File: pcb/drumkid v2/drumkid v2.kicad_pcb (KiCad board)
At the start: 2 copper layers, 0 parts

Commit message: more pcb changes, about to do a big-ish change so doing a commit now
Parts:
- added BT1: Battery, Connector_PinHeader_2.54mm:PinHeader_1x02_P2.54mm_Vertical, F.Cu at (162.0, 128.0)
- added C1: 150uF, Capacitor_THT:CP_Radial_D6.3mm_P2.50mm, F.Cu at (137.0, 64.0)
- added C10: 220uF, Capacitor_THT:CP_Radial_D6.3mm_P2.50mm, F.Cu at (102.0, 71.0)
- added C2: 0.1uF, Capacitor_THT:C_Disc_D3.4mm_W2.1mm_P2.50mm, F.Cu at (150.0, 55.0)
- added C3: 100uF, Capacitor_THT:CP_Radial_D6.3mm_P2.50mm, F.Cu at (137.0, 56.0)
- added C4: 0.1uF, Capacitor_THT:C_Disc_D3.4mm_W2.1mm_P2.50mm, F.Cu at (113.0, 53.0)
- added C5: 10uF, Capacitor_THT:C_Disc_D3.4mm_W2.1mm_P2.50mm, F.Cu at (142.0, 84.0)
- added C6: 10uF, Capacitor_THT:C_Disc_D3.4mm_W2.1mm_P2.50mm, F.Cu at (147.0, 84.0)
- added C7: 10uF, Capacitor_THT:CP_Radial_D6.3mm_P2.50mm, F.Cu at (114.0, 60.0)
- added C8: 100uF, Capacitor_THT:CP_Radial_D6.3mm_P2.50mm, F.Cu at (94.0, 71.0)
- added C9: 0.1uF, Capacitor_THT:C_Disc_D3.4mm_W2.1mm_P2.50mm, F.Cu at (92.0, 79.0)
- added D1: 1N5817, Diode_THT:D_DO-41_SOD81_P10.16mm_Horizontal, F.Cu at (144.0, 65.0)
- added D2: LED, LED_THT:LED_D5.0mm, F.Cu at (151.0, 72.0)
- added D3: LED, LED_THT:LED_D5.0mm, F.Cu at (111.0, 72.0)
- added D4: LED, LED_THT:LED_D5.0mm, F.Cu at (121.0, 72.0)
- added D5: LED, LED_THT:LED_D5.0mm, F.Cu at (131.0, 72.0)
- added D6: LED, LED_THT:LED_D5.0mm, F.Cu at (141.0, 72.0)
- added J1: Conn_01x03_Female, Connector_PinHeader_2.54mm:PinHeader_1x03_P2.54mm_Vertical, F.Cu at (169.0, 67.7)
- added J2: Conn_01x03_Female, Connector_PinHeader_2.54mm:PinHeader_1x03_P2.54mm_Vertical, F.Cu at (154.0, 63.0)
- added J3: Conn_01x03_Female, Connector_PinHeader_2.54mm:PinHeader_1x03_P2.54mm_Vertical, F.Cu at (169.0, 64.0)
- added J4: Conn_01x03_Female, Connector_PinHeader_2.54mm:PinHeader_1x03_P2.54mm_Vertical, F.Cu at (154.1, 66.0)
- added J5: Conn_01x05_Female, Connector_PinHeader_2.54mm:PinHeader_1x05_P2.54mm_Vertical, F.Cu at (122.0, 54.0)
- added J6: Conn_01x04_Female, Connector_PinHeader_2.54mm:PinHeader_1x04_P2.54mm_Vertical, F.Cu at (153.0, 77.0)
- added J7: Conn_01x06_Female, Connector_PinHeader_2.54mm:PinHeader_1x06_P2.54mm_Vertical, F.Cu at (169.0, 61.0)
- added J8: Conn_01x05_Female, Connector_PinHeader_2.54mm:PinHeader_1x05_P2.54mm_Vertical, F.Cu at (169.0, 81.0)
- added J9: AudioJack3_Ground_Switch, headphone:Tayda_3.5mm_stereo_TRS_jack_A-853, F.Cu at (105.0, 38.0)
- added L1: L, Inductor_THT:L_Radial_D6.0mm_P4.00mm, F.Cu at (128.0, 64.0)
- added R1: 470, Resistor_THT:R_Axial_DIN0207_L6.3mm_D2.5mm_P10.16mm_Horizontal, F.Cu at (123.0, 46.0)
- added R10: 100k, Resistor_THT:R_Axial_DIN0207_L6.3mm_D2.5mm_P10.16mm_Horizontal, F.Cu at (97.0, 64.0)
- added R2: 10k, Resistor_THT:R_Axial_DIN0207_L6.3mm_D2.5mm_P10.16mm_Horizontal, F.Cu at (155.0, 45.0)
- added R3: 220, Resistor_THT:R_Axial_DIN0207_L6.3mm_D2.5mm_P10.16mm_Horizontal, F.Cu at (113.0, 87.0)
- added R4: 220, Resistor_THT:R_Axial_DIN0207_L6.3mm_D2.5mm_P10.16mm_Horizontal, F.Cu at (117.0, 87.0)
- added R5: 220, Resistor_THT:R_Axial_DIN0207_L6.3mm_D2.5mm_P10.16mm_Horizontal, F.Cu at (121.0, 87.0)
- added R6: 220, Resistor_THT:R_Axial_DIN0207_L6.3mm_D2.5mm_P10.16mm_Horizontal, F.Cu at (125.0, 87.0)
- added R7: 220, Resistor_THT:R_Axial_DIN0207_L6.3mm_D2.5mm_P10.16mm_Horizontal, F.Cu at (129.0, 77.0)
- added R8: 10, Resistor_THT:R_Axial_DIN0207_L6.3mm_D2.5mm_P10.16mm_Horizontal, F.Cu at (108.0, 79.0)
- added R9: 470k, Resistor_THT:R_Axial_DIN0207_L6.3mm_D2.5mm_P10.16mm_Horizontal, F.Cu at (93.0, 64.0)
- added REF**: MountingHole_3.2mm_M3, MountingHole:MountingHole_3.2mm_M3, F.Cu at (94.0, 39.0)
- added REF**: MountingHole_3.2mm_M3, MountingHole:MountingHole_3.2mm_M3, F.Cu at (171.0, 126.0)
- added REF**: MountingHole_3.2mm_M3, MountingHole:MountingHole_3.2mm_M3, F.Cu at (171.0, 39.0)
- added REF**: MountingHole_3.2mm_M3, MountingHole:MountingHole_3.2mm_M3, F.Cu at (94.0, 126.0)
- added RV1: R_POT, SamacSys_Parts:RK14J12A0A0K, F.Cu at (132.0, 46.0)
- added RV2: R_POT, Potentiometer_THT:Potentiometer_Bourns_PTV09A-1_Single_Vertical, F.Cu at (110.0, 90.0)
- added RV3: R_POT, Potentiometer_THT:Potentiometer_Bourns_PTV09A-1_Single_Vertical, F.Cu at (150.0, 90.0)
- added RV4: R_POT, Potentiometer_THT:Potentiometer_Bourns_PTV09A-1_Single_Vertical, F.Cu at (130.0, 90.0)
- added SW1: SW_SPDT, SamacSys_Parts:EG1206, F.Cu at (160.0, 37.0)
- added SW2: SW_Push, Button_Switch_THT:SW_PUSH-12mm_Wuerth-430476085716, F.Cu at (94.0, 119.0)
- added SW3: SW_Push, Button_Switch_THT:SW_PUSH-12mm_Wuerth-430476085716, F.Cu at (108.0, 119.0)
- added SW4: SW_Push, Button_Switch_THT:SW_PUSH-12mm_Wuerth-430476085716, F.Cu at (140.0, 123.0)
- added SW5: SW_Push, Button_Switch_THT:SW_PUSH-12mm_Wuerth-430476085716, F.Cu at (153.0, 120.0)
- added SW6: SW_Push, Button_Switch_THT:SW_PUSH-12mm_Wuerth-430476085716, F.Cu at (166.0, 117.0)
- added U1: MAX756, Package_DIP:DIP-8_W7.62mm_Socket, F.Cu at (144.0, 51.0)
- added U2: ATmega328P-PU, Package_DIP:DIP-28_W7.62mm_Socket, F.Cu at (158.0, 48.0)
- added U3: LM386, Package_DIP:DIP-8_W7.62mm_Socket, F.Cu at (101.0, 56.0)
- added Y1: Crystal, Crystal:Crystal_HC49-4H_Vertical, F.Cu at (142.0, 80.0)
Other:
- board outline added: 85 x 95 mm

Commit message: good pcb progress, about to make a little change
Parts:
- removed J1, J2, J3, J4: Conn_01x03_Female, Connector_PinHeader_2.54mm:PinHeader_1x03_P2.54mm_Vertical
- added C11: CP, Capacitor_THT:CP_Radial_D6.3mm_P2.50mm, F.Cu at (150.0, 63.0)
- added C12: CP, Capacitor_THT:CP_Radial_D6.3mm_P2.50mm, F.Cu at (143.0, 63.0)
- added C13: 2.2uF, Capacitor_THT:CP_Radial_D6.3mm_P2.50mm, F.Cu at (196.6, 61.4)
- added C14: 220nF, Capacitor_THT:C_Disc_D3.4mm_W2.1mm_P2.50mm, F.Cu at (183.1, 62.4)
- added C15: 10uF, Capacitor_THT:CP_Radial_D6.3mm_P2.50mm, F.Cu at (191.3, 68.3)
- added C16: 100nF, Capacitor_THT:C_Disc_D3.4mm_W2.1mm_P2.50mm, F.Cu at (176.1, 71.9)
- added C17: 10uF, Capacitor_THT:CP_Radial_D6.3mm_P2.50mm, F.Cu at (177.3, 64.5)
- added C18: 100nF, Capacitor_THT:C_Disc_D3.4mm_W2.1mm_P2.50mm, F.Cu at (176.1, 69.2)
- added R11: 10, Resistor_THT:R_Axial_DIN0207_L6.3mm_D2.5mm_P10.16mm_Horizontal, F.Cu at (176.1, 59.5)
- C4, C9: value 0.1uF -> C
- C7: value 10uF -> CP
- C8: value 100uF -> CP
- R1: value 470 -> 47
- R10: value 100k -> 1k
- R8: value 10 -> 470
- R9: value 470k -> 10k
- RV1: value R_POT -> 10k
- moved C8 76.2 mm to (170.0, 76.0)
- moved C9 64.1 mm to (155.0, 67.0), turned to 90 degrees
- moved C4 58.2 mm to (169.0, 69.0), turned to 270 degrees
- moved C7 56.1 mm to (170.0, 64.0)
- moved R9 56.1 mm to (148.0, 53.0)
- moved R10 48.3 mm to (144.0, 53.0)
- moved U3 44.7 mm to (93.0, 100.0), turned to 90 degrees
- moved J5 35.5 mm to (157.0, 48.0), turned to 90 degrees
- moved R8 34.7 mm to (74.0, 86.0)
- moved L1 22.0 mm to (109.0, 53.0)
- moved C1 20.6 mm to (119.0, 54.0), turned to 270 degrees
- moved C3 18.7 mm to (119.0, 61.0), turned to 270 degrees
- moved J6 18.4 mm to (165.0, 91.0)
- moved J8 18.2 mm to (172.0, 99.0)
- moved C2 15.0 mm to (135.0, 55.0), turned to 270 degrees
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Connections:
- C4 pad 2: Net-(C4-Pad2) -> +5V
- C7 pad 1: Net-(C7-Pad1) -> +5V
- C9 pad 1: Net-(C10-Pad1) -> GND
- C9 pad 2: Net-(C9-Pad2) -> +5V
- R1 pad 1: /DIGITAL_9 -> Net-(C13-Pad1)
- R1 pad 2: Net-(C4-Pad2) -> /DIGITAL_9
- R10 pad 1: GND -> Net-(R10-Pad1)
- R10 pad 2: Net-(R10-Pad2) -> GND
- R8 pad 1: GND -> Net-(C14-Pad1)
- R8 pad 2: Net-(C9-Pad2) -> Net-(C13-Pad1)
- R9 pad 1: Net-(C4-Pad2) -> Net-(R10-Pad1)
- R9 pad 2: Net-(R10-Pad2) -> Net-(C15-Pad2)
- RV1 pad 1: GND -> Net-(RV1-Pad1)
- RV1 pad 3: Net-(R10-Pad2) -> Net-(R10-Pad1)
- U3 pad 2: GND -> Net-(RV1-Pad1)
- U3 pad 4: GND -> Net-(C16-Pad2)
- U3 pad 7: Net-(C7-Pad1) -> Net-(C17-Pad2)

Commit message: layout done? ready to route tracks
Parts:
- added J1: Conn_01x04_Female, Connector_PinHeader_2.54mm:PinHeader_1x04_P2.54mm_Vertical, F.Cu at (164.0, 103.0)
- added SW7: SW_Push, Button_Switch_THT:SW_PUSH-12mm_Wuerth-430476085716, F.Cu at (120.0, 120.0)
- moved C17 77.7 mm to (101.0, 79.0)
- moved R9 73.0 mm to (93.0, 101.0), turned to 0 degrees
- moved R8 72.2 mm to (140.4, 57.6), turned to 0 degrees
- moved C16 69.3 mm to (108.0, 85.0)
- moved C18 69.1 mm to (108.0, 81.2)
- moved R11 67.9 mm to (114.0, 87.0), turned to 90 degrees
- moved R10 67.4 mm to (93.0, 97.0), turned to 0 degrees
- moved C15 54.2 mm to (145.0, 40.0), turned to 180 degrees
- moved C13 53.3 mm to (145.0, 48.0), turned to 180 degrees
- moved C14 38.8 mm to (150.0, 42.0), turned to 270 degrees
- moved R1 31.1 mm to (140.4, 53.6), turned to 0 degrees
- moved U3 7.07 mm to (94.0, 93.0)
- moved C5 5.00 mm to (147.0, 84.0)
- moved C6 5.00 mm to (152.0, 84.0)
- moved Y1 5.00 mm to (147.0, 80.0)
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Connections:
- R9 pad 2: Net-(C15-Pad2) -> Net-(R9-Pad2)
- RV1 pad 1: Net-(RV1-Pad1) -> GND
- RV1 pad 2: Net-(RV1-Pad2) -> Net-(R9-Pad2)
- RV1 pad 3: Net-(R10-Pad1) -> Net-(C15-Pad2)
- U3 pad 2: Net-(RV1-Pad1) -> GND
- U3 pad 3: Net-(RV1-Pad2) -> Net-(R10-Pad1)
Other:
- net class Power added: clearance 0.2, trace_width 0.75, via_dia 0.8, via_drill 0.4

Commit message: routing half done maybe
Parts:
- moved SW7 46.0 mm to (166.0, 120.0)
- moved D2 39.0 mm to (112.0, 72.0)
- moved SW4 20.0 mm to (120.0, 120.0)
- moved SW5 13.0 mm to (140.0, 120.0)
- moved SW6 13.0 mm to (153.0, 120.0)
- moved R3 10.4 mm to (122.0, 77.0), turned to 270 degrees
- moved R4 10.4 mm to (126.0, 77.0), turned to 270 degrees
- moved R5 10.4 mm to (130.0, 77.0), turned to 270 degrees
- moved R6 10.4 mm to (134.0, 77.0), turned to 270 degrees
- moved D3 10.0 mm to (121.0, 72.0)
- moved D4 9.00 mm to (130.0, 72.0)
- moved D5 8.00 mm to (139.0, 72.0)
- moved D6 7.00 mm to (148.0, 72.0)
- moved R7 3.00 mm to (138.0, 76.8)
- moved J1 2.00 mm to (162.0, 103.0)
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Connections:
- net Net-(C1-Pad1) renamed /BAT_ON
- C17 pad 1: GND -> Net-(C17-Pad1)
- C17 pad 2: Net-(C17-Pad2) -> GND
- U3 pad 7: Net-(C17-Pad2) -> Net-(C17-Pad1)
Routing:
- net +5V: track 0.00 -> 178.1 mm
- net Net-(BT1-Pad1): track 0.00 -> 110.8 mm
- net /DIGITAL_7: track 0.00 -> 94.8 mm
- net /DIGITAL_10: track 0.00 -> 90.5 mm
- net /DIGITAL_8: track 0.00 -> 81.7 mm
- net GND: track 0.00 -> 75.0 mm
- net Net-(R9-Pad2): track 0.00 -> 73.2 mm
- net /DIGITAL_11: track 0.00 -> 71.4 mm
- net /BAT_ON: track 0.00 -> 62.2 mm
- net Net-(C10-Pad2): track 0.00 -> 52.9 mm
- net /DIGITAL_5: track 0.00 -> 44.5 mm
- net /DIGITAL_6: track 0.00 -> 38.1 mm
- net /DIGITAL_13: track 0.00 -> 30.0 mm
- net /DIGITAL_12: track 0.00 -> 30.0 mm
- net Net-(C14-Pad1): track 0.00 -> 26.3 mm
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
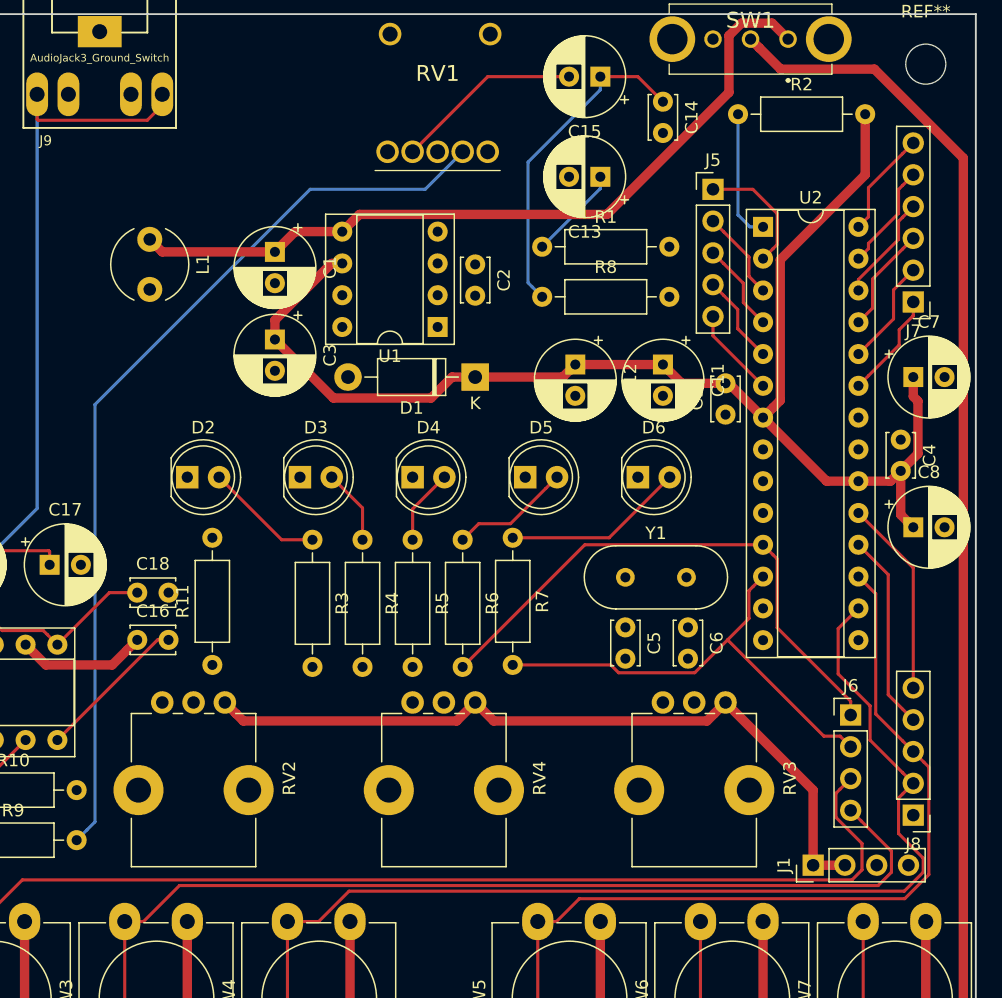
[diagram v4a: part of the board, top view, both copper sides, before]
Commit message: routing nearly done but turns out potentiometer footprint is wrong
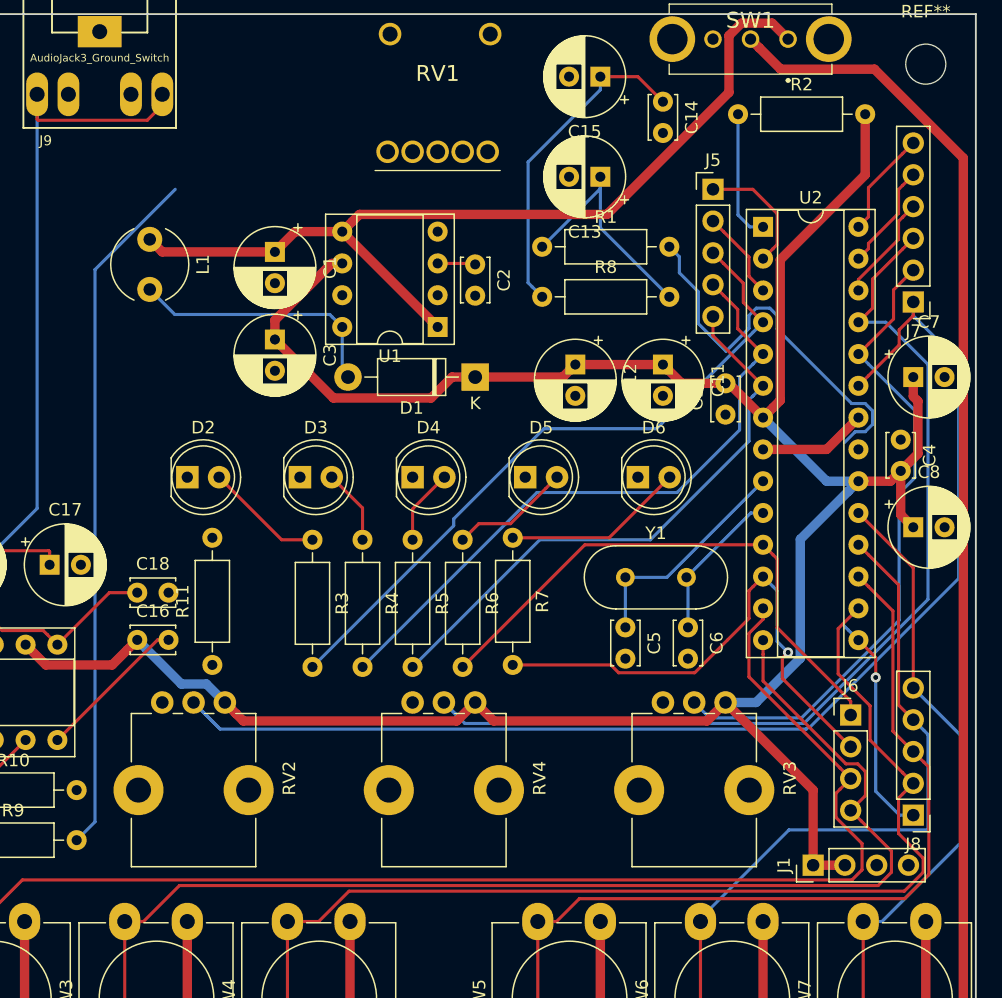
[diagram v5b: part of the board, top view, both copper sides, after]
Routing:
- net /ANALOG_0: track 8.51 -> 101.9 mm
- net /ANALOG_2: track 8.51 -> 79.4 mm
- net /DIGITAL_9: track 0.00 -> 50.0 mm, vias 0 -> 1
- net /DIGITAL_2: track 7.20 -> 54.9 mm
- net /DIGITAL_3: track 7.20 -> 52.0 mm
- net /ANALOG_1: track 8.51 -> 52.3 mm
- net /DIGITAL_4: track 7.20 -> 46.4 mm
- net +5V: track 178.1 -> 210.7 mm
- net /DIGITAL_12: track 30.0 -> 60.6 mm
- net /DIGITAL_13: track 30.0 -> 54.6 mm
- net Net-(D1-Pad2): track 0.00 -> 20.8 mm
- net Net-(C5-Pad1): track 0.00 -> 18.2 mm
- net /DIGITAL_8: track 81.7 -> 99.7 mm
- net Net-(R9-Pad2): track 73.2 -> 55.3 mm
- net /DIGITAL_7: track 94.8 -> 112.2 mm
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
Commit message: 2nd pcb done and sent
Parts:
- removed RV1: 10k, SamacSys_Parts:RK14J12A0A0K
- added J2: Conn_01x05, SamacSys_Parts:RK14J12A0A0K, F.Cu at (131.0, 46.0)
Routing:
- net Net-(J2-Pad3): track 55.3 -> 74.5 mm
- net /DIGITAL_9: track 50.0 -> 63.2 mm
- net Net-(C15-Pad2): track 0.00 -> 9.99 mm
- net Net-(C18-Pad2): track 0.00 -> 7.22 mm
- added copper zone on B.Cu, net GND
- added copper zone on F.Cu, net GND
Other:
- board text added: "DrumKid v02 by Matt Bradshaw mattbradshawdesign.com"
